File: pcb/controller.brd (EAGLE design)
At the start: 55.5 x 38.1 mm, 37 parts, among them IC1 74LS595D, IC2 74LS595D, U1 FT232RLSSOP, U2 ATMEGA328P, X2 USB-SMD-NS

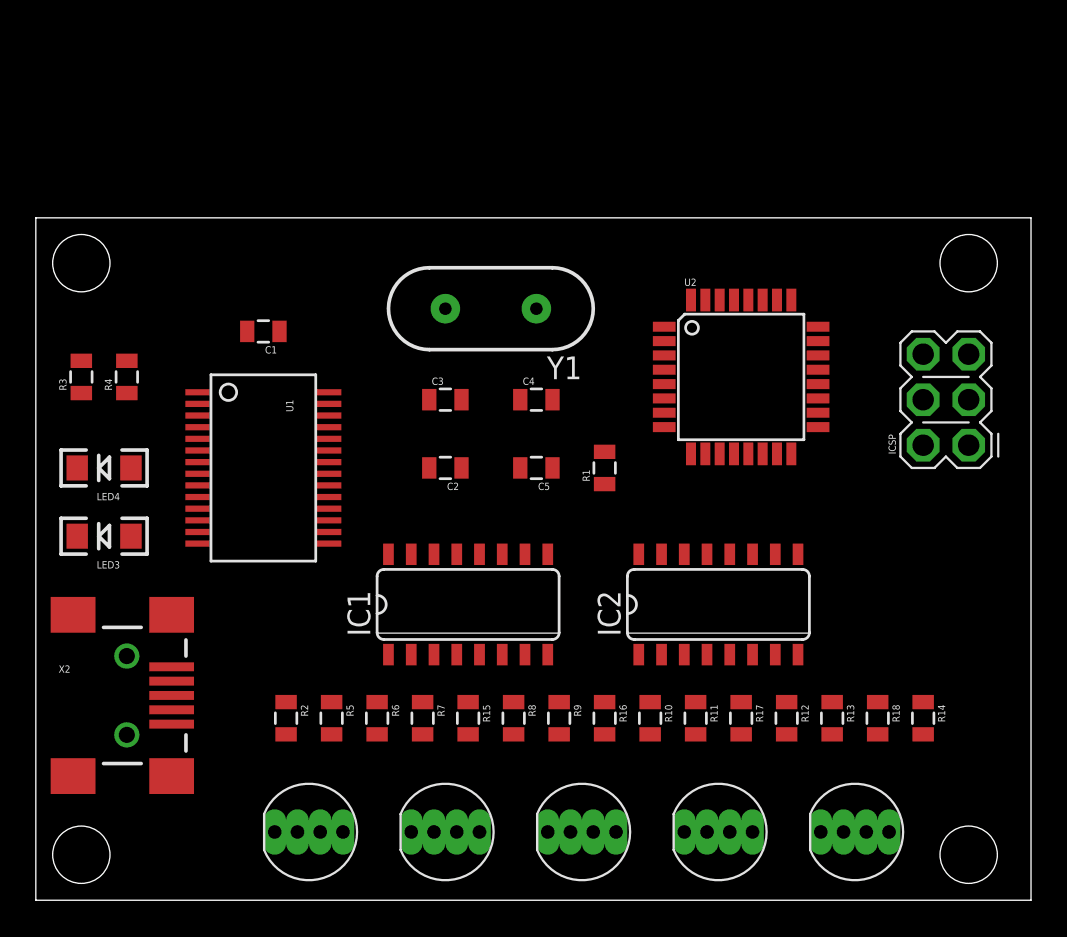
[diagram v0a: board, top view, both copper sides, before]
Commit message: Rearranged board layout
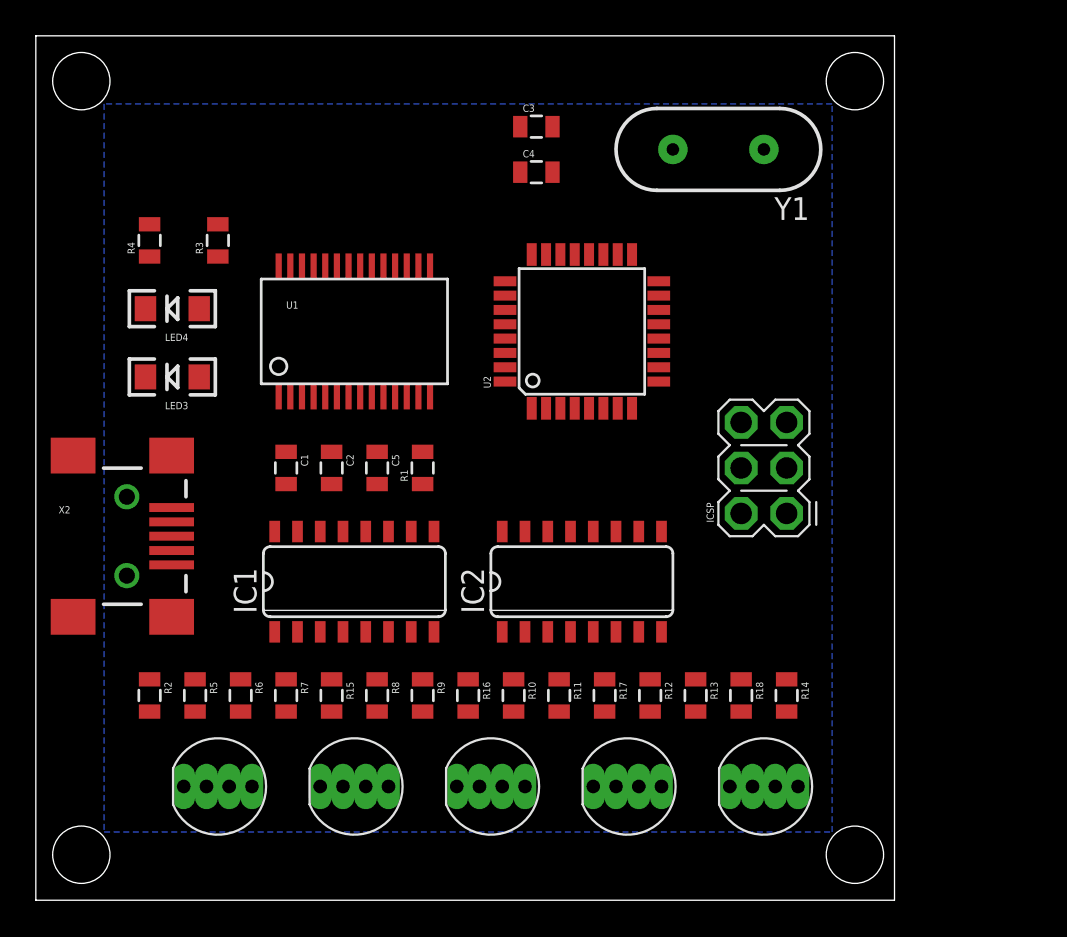
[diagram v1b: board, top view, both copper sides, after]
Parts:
- moved C3 16.1 mm to (27.9, 43.2)
- moved Y1 15.5 mm to (38.1, 41.9)
- moved C4 12.7 mm to (27.9, 40.6)
- moved ICSP 10.9 mm to (41.9, 21.6)
- moved R3 10.8 mm to (10.2, 36.8)
- moved R1 10.2 mm to (21.6, 24.1)
- moved LED4 9.67 mm to (7.62, 33.0)
- moved LED3 9.67 mm to (7.62, 29.2)
- moved U2 9.25 mm to (30.5, 31.8), turned to 90 degrees
- moved U1 9.16 mm to (17.8, 31.8), turned to 0 degrees
- moved C5 8.89 mm to (19.1, 24.1), turned to 270 degrees
- moved X2 8.89 mm to (5.08, 20.3)
- moved R13 7.73 mm to (36.8, 11.4)
- moved R14 7.73 mm to (41.9, 11.4)
- moved R18 7.73 mm to (39.4, 11.4)
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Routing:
- added copper zone on layer 16, net N$24
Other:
- board size 55.5 x 38.1 mm -> 47.9 x 48.2 mm

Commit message: Just before auto route
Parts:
- R10, R11, R12, R13, R14, R15, R16, R17, R18, R5, R6, R7, R8, R9: value 220 -> (none)
- moved C3 20.5 mm to (35.6, 24.1), turned to 90 degrees
- moved C4 17.1 mm to (32.3, 24.1), turned to 90 degrees
- moved Y1 10.5 mm to (40.6, 31.8), turned to 90 degrees
- moved ICSP 5.08 mm to (41.9, 16.5)
- moved LED4 4.06 mm to (7.62, 29.0), turned to 0 degrees
- moved LED3 3.81 mm to (7.62, 33.0), turned to 0 degrees
- moved U1 1.75 mm to (17.8, 33.5)
- moved R3 1.27 mm to (8.89, 36.8)
- moved R4 1.27 mm to (5.08, 36.8)
- moved C1 1.25 mm to (12.7, 24.1)
- moved U2 1.25 mm to (30.5, 33.0)
- moved C2 0.75 mm to (15.8, 24.1)
- moved C5 0.25 mm to (18.8, 24.1)
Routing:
- removed copper zone on layer 16, net N$24
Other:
- board size 47.9 x 48.2 mm -> 47.9 x 42.5 mm
- board text added: "1"
- board text added: "2"
- board text added: "3"
- board text added: "4"
- board text added: "5"
- board text added: "Computer LED Cotroller"
- board text added: "Design By: Eddy Hintze"
- board text added: "RX"
- board text added: "TX"
- board text added: "V1.0"

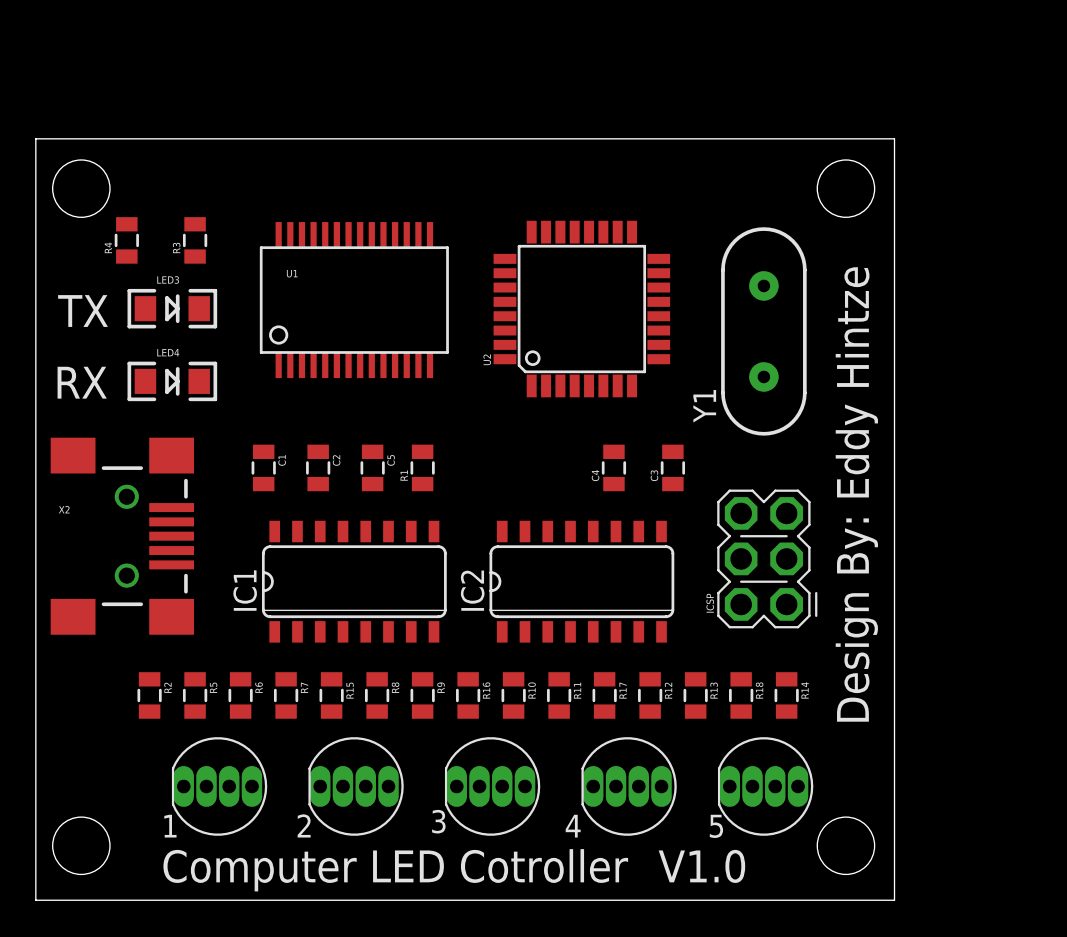
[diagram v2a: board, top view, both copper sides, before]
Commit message: PCB board auto routed
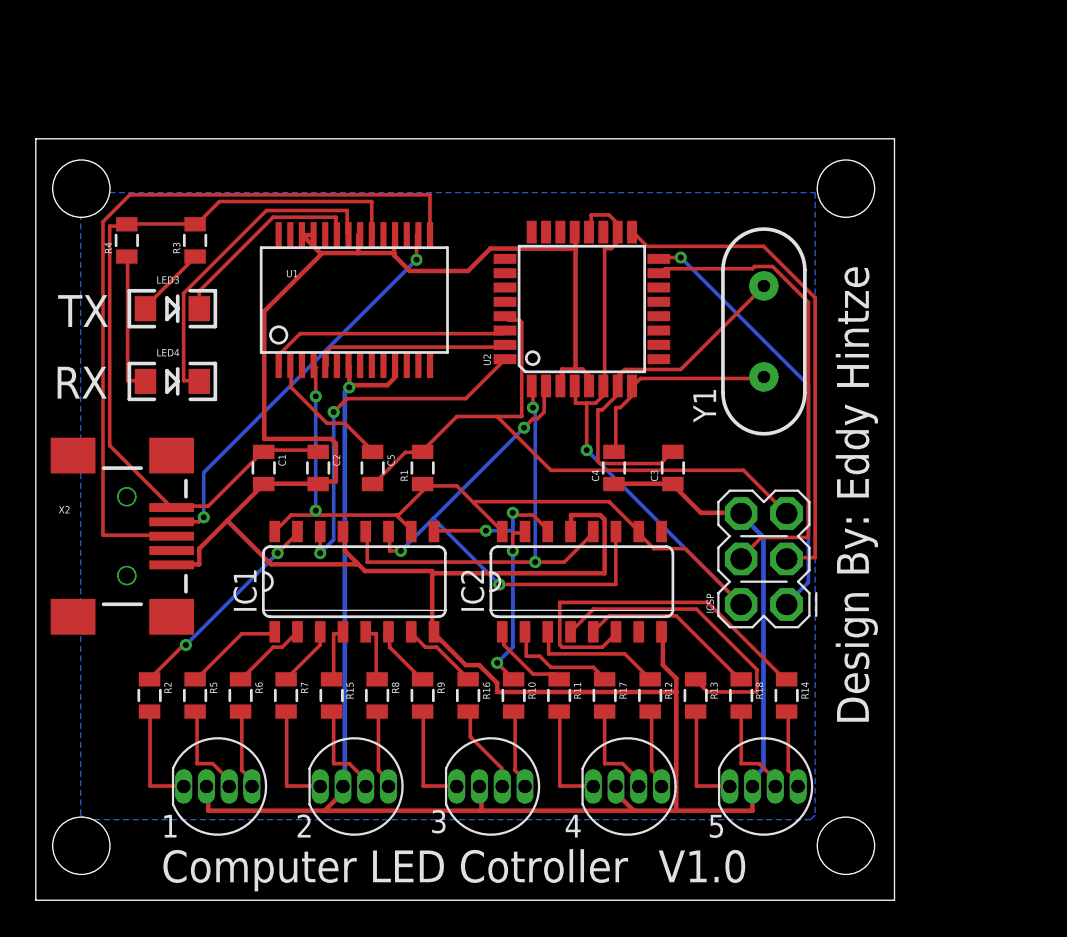
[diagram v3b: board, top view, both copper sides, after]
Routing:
- net GND: track 0.00 -> 208.4 mm, vias 0 -> 1
- net POWER: track 0.00 -> 73.0 mm, vias 0 -> 3
- net 5V: track 0.00 -> 43.8 mm
- net USB_D+: track 0.00 -> 42.4 mm
- net RESET: track 0.00 -> 34.6 mm
- net N$6: track 0.00 -> 29.1 mm, vias 0 -> 3
- net SCK: track 0.00 -> 27.8 mm
- net MOSI: track 0.00 -> 26.8 mm
- net N$5: track 0.00 -> 25.0 mm, vias 0 -> 2
- net MISO: track 0.00 -> 24.1 mm, vias 0 -> 1
- net USB_D-: track 0.00 -> 22.7 mm, vias 0 -> 2
- net LED2G: track 0.00 -> 20.4 mm
- net N$4: track 0.00 -> 20.2 mm, vias 0 -> 2
- net N$7: track 0.00 -> 20.1 mm
- net RXLED: track 0.00 -> 18.2 mm
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- added copper zone on layer 16, net GND
